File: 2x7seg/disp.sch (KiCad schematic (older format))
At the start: 9 parts, among them P1 CONN_01X08, P2 CONN_01X08, U1 TLC59282

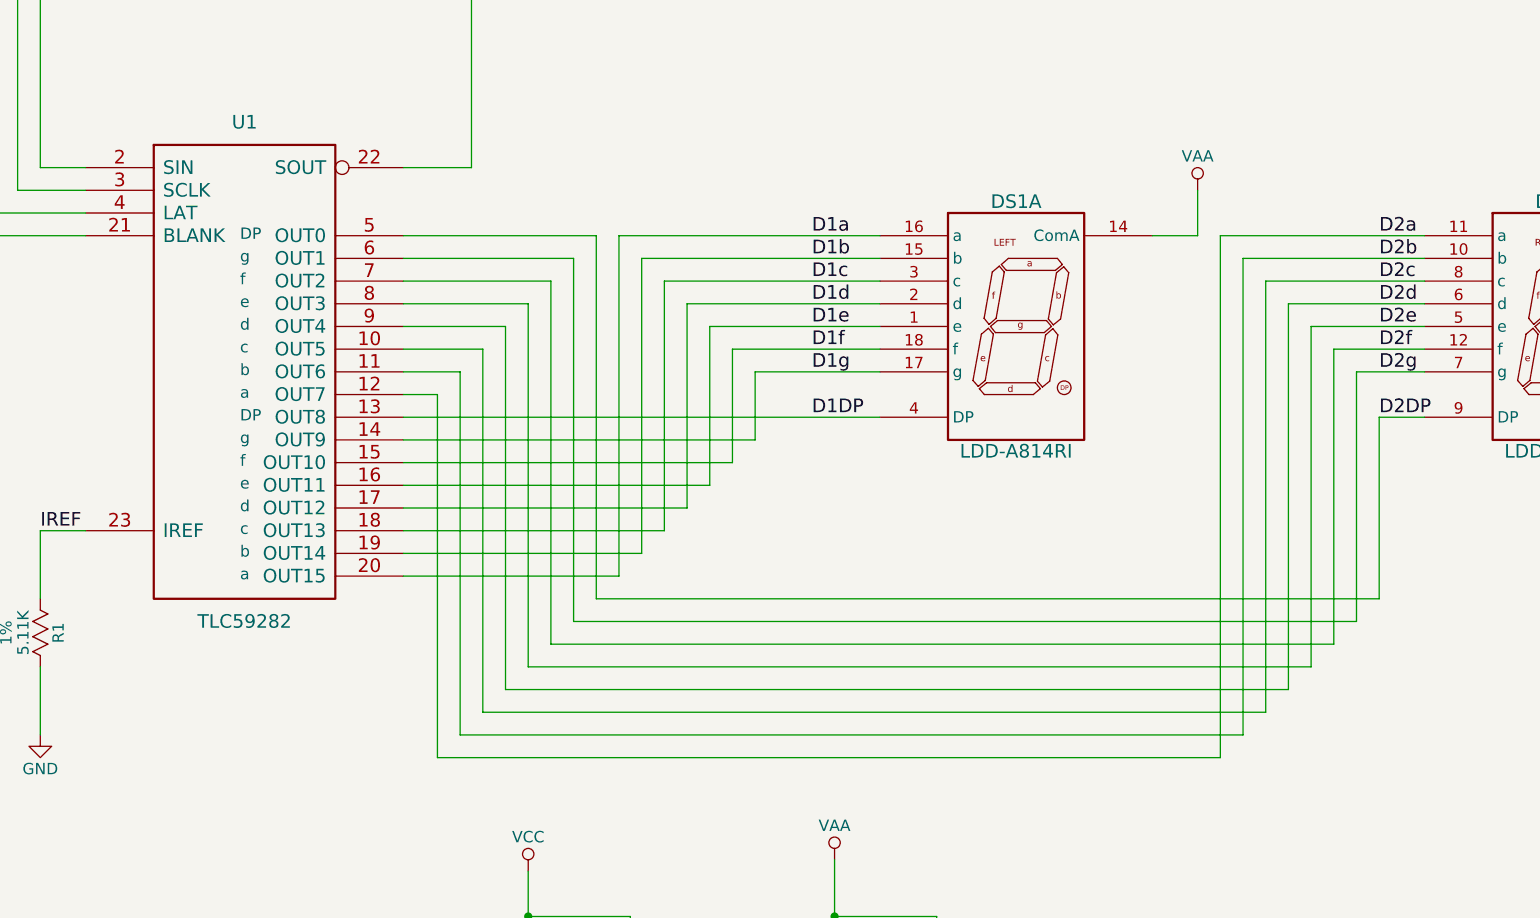
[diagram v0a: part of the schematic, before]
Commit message: Make schematic for the display board more readable.
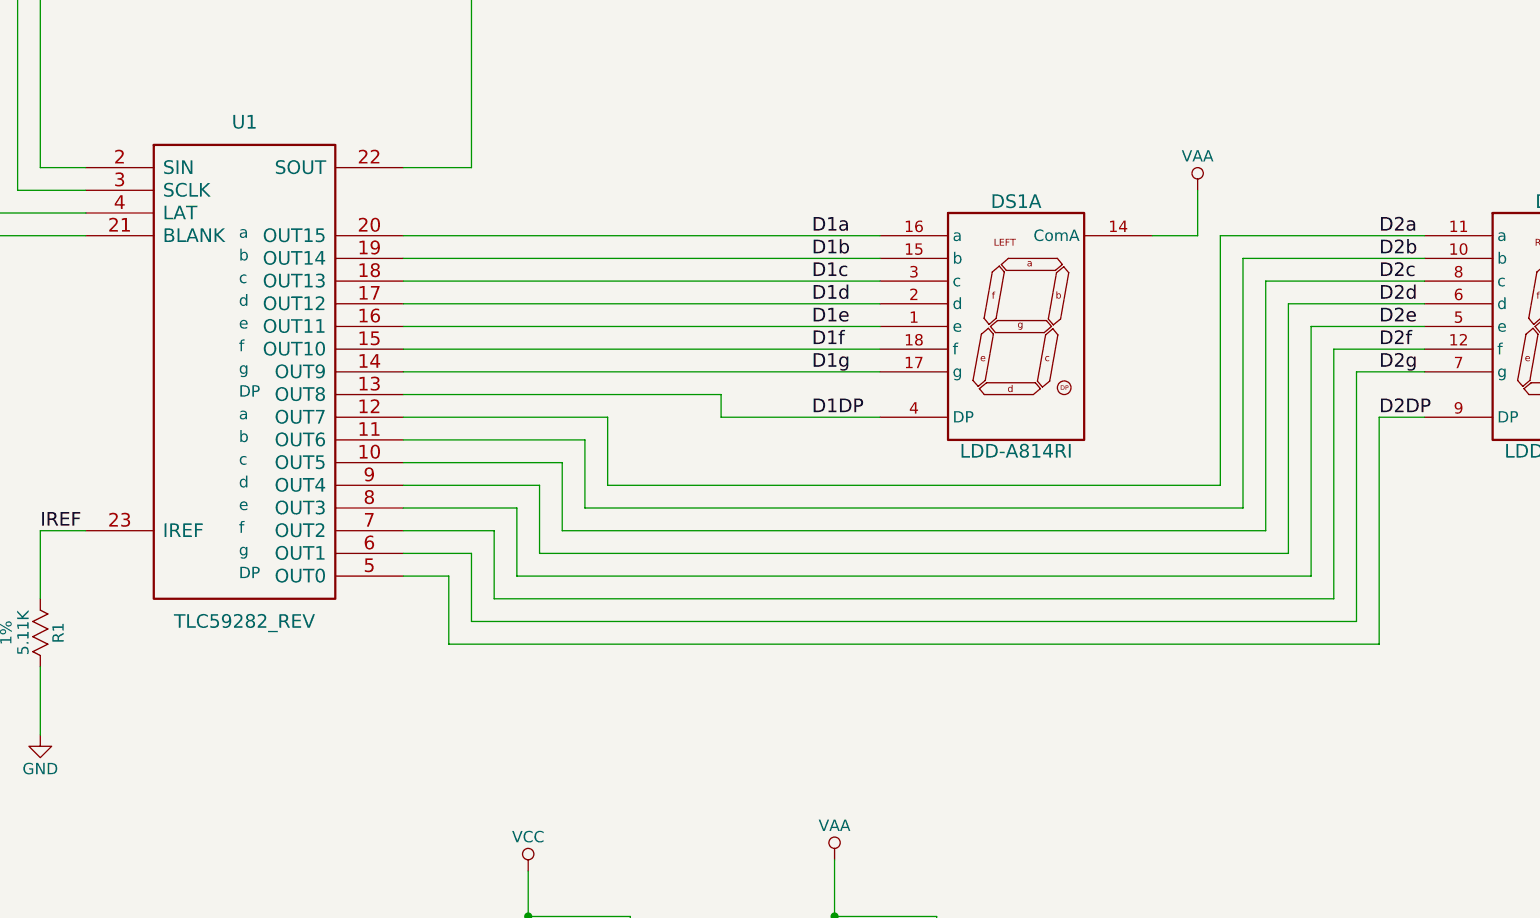
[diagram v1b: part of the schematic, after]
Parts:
- removed U1: TLC59282, local:SOIC-24_6.0x8.65mm_Pitch25mil, symbol TLC59282
- added U1: TLC59282_REV, local:SOIC-24_6.0x8.65mm_Pitch25mil, symbol TLC59282_REV
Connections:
- net BLANK: now also U1.21 (BLANK)
- net D1DP: now also U1.13 (OUT8)
- net D1a: now also U1.20 (OUT15)
- net D1b: now also U1.19 (OUT14)
- net D1c: now also U1.18 (OUT13)
- net D1d: now also U1.17 (OUT12)
- net D1e: now also U1.16 (OUT11)
- net D1f: now also U1.15 (OUT10)
- net D1g: now also U1.14 (OUT9)
- net D2DP: now also U1.5 (OUT0)
- net D2a: now also U1.12 (OUT7)
- net D2b: now also U1.11 (OUT6)
- net D2c: now also U1.10 (OUT5)
- net D2d: now also U1.9 (OUT4)
- net D2e: now also U1.8 (OUT3)
- net D2f: now also U1.7 (OUT2)
- net D2g: now also U1.6 (OUT1)
- net GND: now also U1.1 (GND)
- net IREF: now also U1.23 (IREF)
- net LAT: now also U1.4 (LAT)
- net SCLK: now also U1.3 (SCLK)
- net SIN: now also U1.2 (SIN)
- net SOUT: now also U1.22 (SOUT)
- net VCC: now also U1.24 (VCC)
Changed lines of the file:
@@
 Connection ~ 4450 6600
 Wire Wire Line
-	3900 5100 4850 5100
-Wire Wire Line
-	4850 5100 4850 3600
-Wire Wire Line
-	4850 3600 6000 3600
-Wire Wire Line
-	3900 5000 4950 5000
-Wire Wire Line
-	4950 5000 4950 3700
-Wire Wire Line
-	5050 3800 5050 4900
-Wire Wire Line
-	5050 4900 3900 4900
-Wire Wire Line
-	3900 4800 5150 4800
-Wire Wire Line
-	5150 4800 5150 3900
-Wire Wire Line
-	5150 3900 6000 3900
-Wire Wire Line
-	6000 4000 5250 4000
-Wire Wire Line
-	5250 4000 5250 4700
-Wire Wire Line
-	5250 4700 3900 4700
-Wire Wire Line
-	3900 4600 5350 4600
-Wire Wire Line
-	5350 4600 5350 4100
-Wire Wire Line
-	5350 4100 6000 4100
-Wire Wire Line
-	6000 4200 5450 4200
-Wire Wire Line
-	5450 4200 5450 4500
-Wire Wire Line
-	5450 4500 3900 4500
-Wire Wire Line
-	3900 4400 6000 4400
-Wire Wire Line
-	3900 4300 4050 4300
-Wire Wire Line
-	4050 4300 4050 5900
-Wire Wire Line
-	4050 5900 7500 5900
-Wire Wire Line
-	7500 5900 7500 3600
+	3900 3600 6000 3600
+Wire Wire Line
+	3900 3700 6000 3700
+Wire Wire Line
+	3900 3800 6000 3800
+Wire Wire Line
+	3900 3900 6000 3900
+Wire Wire Line
+	3900 4000 6000 4000
+Wire Wire Line
+	3900 4100 6000 4100
+Wire Wire Line
+	3900 4200 6000 4200
+Wire Wire Line
+	3900 4400 4800 4400
+Wire Wire Line
+	4800 4400 4800 4700
+Wire Wire Line
+	4800 4700 7500 4700
+Wire Wire Line
+	7500 4700 7500 3600
 Wire Wire Line
 	7500 3600 8400 3600
 Wire Wire Line
-	3900 4200 4150 4200
-Wire Wire Line
-	4150 4200 4150 5800
-Wire Wire Line
-	4150 5800 7600 5800
-Wire Wire Line
-	7600 5800 7600 3700
+	3900 4500 4700 4500
+Wire Wire Line
+	4700 4500 4700 4800
+Wire Wire Line
+	4700 4800 7600 4800
+Wire Wire Line
+	7600 4800 7600 3700
 Wire Wire Line
 	7600 3700 8400 3700
 Wire Wire Line
-	3900 4100 4250 4100
-Wire Wire Line
-	4250 4100 4250 5700
-Wire Wire Line
-	4250 5700 7700 5700
-Wire Wire Line
-	7700 5700 7700 3800
+	3900 4600 4600 4600
+Wire Wire Line
+	4600 4600 4600 4900
+Wire Wire Line
+	4600 4900 7700 4900
+Wire Wire Line
+	7700 4900 7700 3800
 Wire Wire Line
 	7700 3800 8400 3800
 Wire Wire Line
-	3900 4000 4350 4000
-Wire Wire Line
-	4350 4000 4350 5600
-Wire Wire Line
-	4350 5600 7800 5600
-Wire Wire Line
-	7800 5600 7800 3900
+	3900 4700 4500 4700
+Wire Wire Line
+	4500 4700 4500 5000
+Wire Wire Line
+	4500 5000 7800 5000
+Wire Wire Line
+	7800 5000 7800 3900
 Wire Wire Line
 	7800 3900 8400 3900
@@
 	8400 4000 7900 4000
 Wire Wire Line
-	7900 4000 7900 5500
-Wire Wire Line
-	7900 5500 4450 5500
-Wire Wire Line
-	4450 5500 4450 3900
-Wire Wire Line
-	4450 3900 3900 3900
-Wire Wire Line
-	3900 3800 4550 3800
-Wire Wire Line
-	4550 3800 4550 5400
-Wire Wire Line
-	4550 5400 8000 5400
-Wire Wire Line
-	8000 5400 8000 4100
+	7900 4000 7900 5100
+Wire Wire Line
+	7900 5100 4400 5100
+Wire Wire Line
+	4400 5100 4400 4800
+Wire Wire Line
+	4400 4800 3900 4800
+Wire Wire Line
+	3900 4900 4300 4900
+Wire Wire Line
+	4300 4900 4300 5200
+Wire Wire Line
+	4300 5200 8000 5200
+Wire Wire Line
+	8000 5200 8000 4100
 Wire Wire Line
 	8000 4100 8400 4100
@@
 	8100 4200 8100 5300
 Wire Wire Line
-	8100 5300 4650 5300
-Wire Wire Line
-	4650 5300 4650 3700
-Wire Wire Line
-	4650 3700 3900 3700
-Wire Wire Line
-	3900 3600 4750 3600
-Wire Wire Line
-	4750 3600 4750 5200
-Wire Wire Line
-	4750 5200 8200 5200
-Wire Wire Line
-	8200 5200 8200 4400
+	8100 5300 4200 5300
+Wire Wire Line
+	4200 5300 4200 5000
+Wire Wire Line
+	4200 5000 3900 5000
+Wire Wire Line
+	3900 5100 4100 5100
+Wire Wire Line
+	4100 5100 4100 5400
+Wire Wire Line
+	4100 5400 8200 5400
+Wire Wire Line
+	8200 5400 8200 4400
 Wire Wire Line
 	8200 4400 8400 4400
@@
 Connection ~ 5750 2500
 Connection ~ 4700 1800
-Wire Wire Line
-	4950 3700 6000 3700
-Wire Wire Line
-	6000 3800 5050 3800
 Text Label 7100 2100 0    60   ~ 0
 SOUT
@@
 $EndComp
 $Comp
-L TLC59282 U1
-U 1 1 562D2ACF
-P 3200 4200
-F 0 "U1" H 3200 5300 60  0000 C CNN
-F 1 "TLC59282" H 3200 3100 60  0000 C CNN
-F 2 "local:SOIC-24_6.0x8.65mm_Pitch25mil" H 3200 4000 60  0001 C CNN
-F 3 "" H 3200 4000 60  0000 C CNN
-F 4 "Texas Instruments" H 3200 4200 50  0001 C CNN "Manufacturer"
-F 5 "TLC59282DBQ" H 3200 3000 50  0001 C CNN "PartNum"
-	1    3200 4200
-	1    0    0    -1
-$EndComp
-$Comp
 L C C4
 U 1 1 562F02F5
@@
 	1    0    0    -1
 $EndComp
-Text Notes 3180 5130 0    50   ~ 0
+Text Notes 3175 3625 0    50   ~ 0
 a
-Text Notes 3180 5030 0    50   ~ 0
+Text Notes 3175 3725 0    50   ~ 0
 b
-Text Notes 3180 4930 0    50   ~ 0
+Text Notes 3175 3825 0    50   ~ 0
 c
-Text Notes 3180 4830 0    50   ~ 0
+Text Notes 3175 3925 0    50   ~ 0
 d
-Text Notes 3180 4730 0    50   ~ 0
+Text Notes 3175 4025 0    50   ~ 0
 e
-Text Notes 3180 4630 0    50   ~ 0
+Text Notes 3175 4125 0    50   ~ 0
 f
-Text Notes 3180 4530 0    50   ~ 0
+Text Notes 3175 4225 0    50   ~ 0
 g
-Text Notes 3180 4430 0    50   ~ 0
+Text Notes 3175 4325 0    50   ~ 0
 DP
-Text Notes 3180 4330 0    50   ~ 0
+Text Notes 3175 4425 0    50   ~ 0
 a
-Text Notes 3180 4230 0    50   ~ 0
+Text Notes 3175 4525 0    50   ~ 0
 b
-Text Notes 3180 4130 0    50   ~ 0
+Text Notes 3175 4625 0    50   ~ 0
 c
-Text Notes 3180 4030 0    50   ~ 0
+Text Notes 3175 4725 0    50   ~ 0
 d
-Text Notes 3180 3930 0    50   ~ 0
+Text Notes 3175 4825 0    50   ~ 0
 e
-Text Notes 3180 3830 0    50   ~ 0
+Text Notes 3175 4925 0    50   ~ 0
 f
-Text Notes 3180 3730 0    50   ~ 0
+Text Notes 3175 5025 0    50   ~ 0
 g
-Text Notes 3180 3630 0    50   ~ 0
+Text Notes 3175 5125 0    50   ~ 0
 DP
+$Comp
+L TLC59282_REV U1
+U 1 1 58F163E9
+P 3200 4200
+F 0 "U1" H 3200 5300 60  0000 C CNN
+F 1 "TLC59282_REV" H 3200 3100 60  0000 C CNN
+F 2 "local:SOIC-24_6.0x8.65mm_Pitch25mil" H 3200 4000 60  0001 C CNN
+F 3 "" H 3200 4000 60  0000 C CNN
+F 4 "Texas Instruments" H 3200 3025 50  0001 C CNN "Manufacturer"
+F 5 "TLC59282DBQ" H 3200 2925 50  0001 C CNN "PartNum"
+	1    3200 4200
+	1    0    0    -1
+$EndComp
+Wire Wire Line
+	3900 4300 5300 4300
+Wire Wire Line
+	5300 4300 5300 4400
+Wire Wire Line
+	5300 4400 6000 4400
 $EndSCHEMATC

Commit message: Update display board to kicad 5.1. Regenerate output files.
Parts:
- C1, C2, C3, C4: symbol C -> device:C
- DS1: symbol LDD-A814RI -> Local:LDD-A814RI
- P1, P2: symbol CONN_01X08 -> conn:CONN_01X08
- R1: symbol R_local -> Local:R_local
- U1: symbol TLC59282_REV -> Local:TLC59282_REV
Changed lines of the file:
@@
-EESchema Schematic File Version 2
-LIBS:power
-LIBS:device
-LIBS:transistors
-LIBS:conn
-LIBS:linear
-LIBS:regul
-LIBS:74xx
-LIBS:cmos4000
-LIBS:adc-dac
-LIBS:memory
-LIBS:xilinx
-LIBS:microcontrollers
-LIBS:dsp
-LIBS:microchip
-LIBS:analog_switches
-LIBS:motorola
-LIBS:texas
-LIBS:intel
-LIBS:audio
-LIBS:interface
-LIBS:digital-audio
-LIBS:philips
-LIBS:display
-LIBS:cypress
-LIBS:siliconi
-LIBS:opto
-LIBS:atmel
-LIBS:contrib
-LIBS:valves
-LIBS:local
-LIBS:disp-cache
-EELAYER 25 0
+EESchema Schematic File Version 4
+EELAYER 30 0
 EELAYER END
 $Descr A4 11693 8268
@@
 $EndDescr
 $Comp
-L CONN_01X08 P1
+L conn:CONN_01X08 P1
 U 1 1 5597595F
 P 1200 2150
@@
 $EndComp
 $Comp
-L CONN_01X08 P2
+L conn:CONN_01X08 P2
 U 1 1 559759A0
 P 10500 2150
@@
 $EndComp
 $Comp
-L C C1
+L device:C C1
 U 1 1 559759DC
 P 4450 6900
@@
 $EndComp
 $Comp
-L C C2
+L device:C C2
 U 1 1 55975A79
 P 4900 6900
@@
 $EndComp
 $Comp
-L C C3
+L device:C C3
 U 1 1 55975AC9
 P 5800 6900
@@
 $EndComp
 $Comp
-L GND #PWR01
+L power:GND #PWR01
 U 1 1 55975CA2
 P 2300 5800
@@
 $EndComp
 $Comp
-L VCC #PWR02
+L power:VCC #PWR02
 U 1 1 55975CC2
 P 1800 1500
@@
 $EndComp
 Wire Wire Line
-	1400 1800 10300 1800
-Wire Wire Line
-	1400 1900 10300 1900
-Wire Wire Line
-	1400 2000 10300 2000
-Wire Wire Line
-	1400 2200 10300 2200
-Wire Wire Line
-	1400 2300 10300 2300
-Wire Wire Line
-	1400 2400 10300 2400
-Wire Wire Line
-	1400 2500 10300 2500
-Wire Wire Line
-	4450 6400 4450 6750
+	1400 1800 3200 1800
+Wire Wire Line
+	1400 1900 1800 1900
+Wire Wire Line
+	1400 2000 1550 2000
+Wire Wire Line
+	1400 2200 2100 2200
+Wire Wire Line
+	1400 2300 2000 2300
+Wire Wire Line
+	1400 2400 2200 2400
+Wire Wire Line
+	1400 2500 1550 2500
+Wire Wire Line
+	4450 6400 4450 6600
 Wire Wire Line
 	4450 6600 4900 6600
@@
 	4900 6600 4900 6750
 Wire Wire Line
-	4450 7050 4450 7400
+	4450 7050 4450 7200
 Wire Wire Line
 	4450 7200 4900 7200
@@
 	4900 7200 4900 7050
 Wire Wire Line
-	5800 6350 5800 6750
+	5800 6350 5800 6600
 Wire Wire Line
 	5800 6600 6250 6600
@@
 	6250 7200 5800 7200
 Wire Wire Line
-	5800 7050 5800 7400
-$Comp
-L GND #PWR03
+	5800 7050 5800 7200
+$Comp
+L power:GND #PWR03
 U 1 1 5597FD15
 P 1800 2750
@@
 	2300 5500 2300 5800
 $Comp
-L GND #PWR04
+L power:GND #PWR04
 U 1 1 55980AD7
 P 4450 7400
@@
 Connection ~ 4450 7200
 $Comp
-L GND #PWR05
+L power:GND #PWR05
 U 1 1 55980ED3
 P 5800 7400
@@
 Connection ~ 5800 7200
 $Comp
-L VCC #PWR06
+L power:VCC #PWR06
 U 1 1 55981037
 P 4450 6400
@@
 	8200 4400 8400 4400
 $Comp
-L VAA #PWR07
+L power:VAA #PWR07
 U 1 1 559831F1
 P 3200 1500
@@
 $EndComp
 $Comp
-L VAA #PWR08
+L power:VAA #PWR08
 U 1 1 559832E2
 P 9800 3400
@@
 	9800 3600 9600 3600
 $Comp
-L VAA #PWR09
+L power:VAA #PWR09
 U 1 1 559842A3
 P 5800 6350
@@
 Connection ~ 5800 6600
 $Comp
-L VAA #PWR010
+L power:VAA #PWR010
 U 1 1 559843C1
 P 7400 3400
@@
 	7400 3600 7200 3600
 $Comp
-L PWR_FLAG #FLG011
+L power:PWR_FLAG #FLG011
 U 1 1 559854F7
 P 4700 1500
@@
 	4700 1500 4700 1800
 $Comp
-L PWR_FLAG #FLG012
+L power:PWR_FLAG #FLG012
 U 1 1 55985759
 P 5250 1500
@@
 $EndComp
 $Comp
-L PWR_FLAG #FLG013
+L power:PWR_FLAG #FLG013
 U 1 1 5598594E
 P 5750 1500
@@
 Connection ~ 1550 2000
 $Comp
-L R_local R1
+L Local:R_local R1
 U 1 1 562D2422
 P 2300 5350
@@
 $EndComp
 $Comp
-L C C4
+L device:C C4
 U 1 1 562F02F5
 P 6250 6900
@@
 $EndComp
 $Comp
-L LDD-A814RI DS1
+L Local:LDD-A814RI DS1
 U 2 1 562F101C
 P 9000 4000
@@
 $EndComp
 $Comp
-L LDD-A814RI DS1
+L Local:LDD-A814RI DS1
 U 1 1 562F11DB
 P 6600 4000
@@
 DP
 $Comp
-L TLC59282_REV U1
+L Local:TLC59282_REV U1
 U 1 1 58F163E9
 P 3200 4200
@@
 Wire Wire Line
 	5300 4400 6000 4400
+Wire Wire Line
+	1800 2500 5750 2500
+Wire Wire Line
+	2200 2400 10300 2400
+Wire Wire Line
+	2100 2200 10300 2200
+Wire Wire Line
+	2000 2300 10300 2300
+Wire Wire Line
+	4450 7200 4450 7400
+Wire Wire Line
+	5800 7200 5800 7400
+Wire Wire Line
+	4450 6600 4450 6750
+Wire Wire Line
+	5800 6600 5800 6750
+Wire Wire Line
+	5250 1900 10300 1900
+Wire Wire Line
+	5750 2500 10300 2500
+Wire Wire Line
+	4700 1800 10300 1800
+Wire Wire Line
+	3200 1800 4700 1800
+Wire Wire Line
+	1800 1900 5250 1900
+Wire Wire Line
+	1550 2500 1800 2500
+Wire Wire Line
+	1550 2000 10300 2000
 $EndSCHEMATC

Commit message: Fix display board to point to 5.1 symbol libraries.
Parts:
- C1, C2, C3, C4: symbol device:C -> Device:C
- P1, P2: symbol conn:CONN_01X08 -> Connector_Generic:Conn_01x08
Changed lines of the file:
@@
 $EndDescr
 $Comp
-L conn:CONN_01X08 P1
+L Connector_Generic:Conn_01x08 P1
 U 1 1 5597595F
-P 1200 2150
-F 0 "P1" H 1200 2600 50  0000 C CNN
-F 1 "CONN_01X08" V 1300 2150 50  0000 C CNN
-F 2 "local:Pin_Header_1x08_edge" H 1200 2150 60  0001 C CNN
-F 3 "" H 1200 2150 60  0000 C CNN
-	1    1200 2150
+P 1200 2100
+F 0 "P1" H 1200 2550 50  0000 C CNN
+F 1 "CONN_01X08" V 1300 2100 50  0000 C CNN
+F 2 "local:Pin_Header_1x08_edge" H 1200 2100 60  0001 C CNN
+F 3 "" H 1200 2100 60  0000 C CNN
+	1    1200 2100
 	-1   0    0    -1
 $EndComp
 $Comp
-L conn:CONN_01X08 P2
+L Connector_Generic:Conn_01x08 P2
 U 1 1 559759A0
-P 10500 2150
-F 0 "P2" H 10500 2600 50  0000 C CNN
-F 1 "CONN_01X08" V 10600 2150 50  0000 C CNN
-F 2 "local:Pin_Header_1x08_edge" H 10500 2150 60  0001 C CNN
-F 3 "" H 10500 2150 60  0000 C CNN
-	1    10500 2150
+P 10500 2200
+F 0 "P2" H 10500 2650 50  0000 C CNN
+F 1 "CONN_01X08" V 10600 2200 50  0000 C CNN
+F 2 "local:Pin_Header_1x08_edge" H 10500 2200 60  0001 C CNN
+F 3 "" H 10500 2200 60  0000 C CNN
+	1    10500 2200
 	1    0    0    1
 $EndComp
 $Comp
-L device:C C1
+L Device:C C1
 U 1 1 559759DC
 P 4450 6900
@@
 $EndComp
 $Comp
-L device:C C2
+L Device:C C2
 U 1 1 55975A79
 P 4900 6900
@@
 $EndComp
 $Comp
-L device:C C3
+L Device:C C3
 U 1 1 55975AC9
 P 5800 6900
@@
 $EndComp
 $Comp
-L device:C C4
+L Device:C C4
 U 1 1 562F02F5
 P 6250 6900
